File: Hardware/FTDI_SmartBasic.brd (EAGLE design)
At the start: 35.6 x 20.3 mm, 27 parts, among them U1 FT232RLSSOP, U2 MIC5219 3.3V, U3 TS3USB221A

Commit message: Ready for release.
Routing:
- net !OE: track 14.0 -> 16.4 mm
- net N$17: track 16.9 -> 15.9 mm
- net N$16: track 19.7 -> 18.9 mm
- net GND: vias 10 -> 9
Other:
- board text added: "HOST/!USB"
- board text removed: "AUX/!USB"
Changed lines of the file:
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@@
 <grid distance="0.05" unitdist="inch" unit="inch" style="lines" multiple="1" display="yes" altdistance="0.005" altunitdist="inch" altunit="inch"/>
 <layers>
-<layer number="1" name="Top" color="4" fill="1" visible="yes" active="yes"/>
+<layer number="1" name="Top" color="4" fill="1" visible="no" active="yes"/>
 <layer number="2" name="Route2" color="1" fill="3" visible="no" active="yes"/>
 <layer number="15" name="Route15" color="4" fill="6" visible="no" active="yes"/>
@@
 <layer number="19" name="Unrouted" color="6" fill="1" visible="yes" active="yes"/>
 <layer number="20" name="Dimension" color="15" fill="1" visible="yes" active="yes"/>
-<layer number="21" name="tPlace" color="16" fill="1" visible="yes" active="yes"/>
+<layer number="21" name="tPlace" color="16" fill="1" visible="no" active="yes"/>
 <layer number="22" name="bPlace" color="14" fill="1" visible="yes" active="yes"/>
-<layer number="23" name="tOrigins" color="15" fill="1" visible="yes" active="yes"/>
+<layer number="23" name="tOrigins" color="15" fill="1" visible="no" active="yes"/>
 <layer number="24" name="bOrigins" color="15" fill="1" visible="yes" active="yes"/>
 <layer number="25" name="tNames" color="7" fill="1" visible="no" active="yes"/>
@@
 <layer number="43" name="vRestrict" color="2" fill="10" visible="no" active="yes"/>
 <layer number="44" name="Drills" color="7" fill="1" visible="no" active="yes"/>
-<layer number="45" name="Holes" color="7" fill="1" visible="yes" active="yes"/>
+<layer number="45" name="Holes" color="7" fill="1" visible="no" active="yes"/>
 <layer number="46" name="Milling" color="3" fill="1" visible="no" active="yes"/>
-<layer number="51" name="tDocu" color="6" fill="1" visible="yes" active="yes"/>
+<layer number="51" name="tDocu" color="6" fill="1" visible="no" active="yes"/>
 <layer number="52" name="bDocu" color="7" fill="1" visible="no" active="yes"/>
 <layer number="3" name="Route3" color="4" fill="3" visible="no" active="no"/>
@@
 <text x="26.797" y="11.938" size="0.8636" layer="21" font="vector" ratio="15" align="bottom-center">TX</text>
 <text x="24.765" y="11.938" size="0.8636" layer="21" font="vector" ratio="15" align="bottom-center">RX</text>
-<text x="27.94" y="6.35" size="1.016" layer="21" font="vector" ratio="15" rot="R180" align="bottom-center">AUX/!USB</text>
+<text x="27.94" y="6.35" size="1.016" layer="21" font="vector" ratio="15" rot="R180" align="bottom-center">HOST/!USB</text>
 <text x="27.94" y="3.048" size="0.8636" layer="21" font="vector" ratio="15" align="bottom-center">SEL</text>
 <text x="30.48" y="3.048" size="0.8636" layer="21" font="vector" ratio="15" align="bottom-center">!OE</text>
@@
 <via x="17.526" y="15.367" extent="1-16" drill="0.508"/>
 <via x="5.842" y="16.256" extent="1-16" drill="0.508"/>
-<via x="15.621" y="17.907" extent="1-16" drill="0.508"/>
+<via x="15.24" y="17.78" extent="1-16" drill="0.508"/>
 <via x="15.494" y="8.001" extent="1-16" drill="0.508"/>
 <contactref element="R3" pad="1"/>
 <contactref element="R5" pad="1"/>
 <contactref element="C6" pad="2"/>
-<via x="26.543" y="5.969" extent="1-16" drill="0.508"/>
 <via x="28.067" y="10.033" extent="1-16" drill="0.508"/>
 </signal>
@@
 <contactref element="R1" pad="2"/>
 <contactref element="R2" pad="2"/>
-<wire x1="13.97" y1="16.93" x2="18.415" y2="17.018" width="0.254" layer="1"/>
-<wire x1="18.415" y1="17.018" x2="18.962" y2="17.565" width="0.254" layer="1"/>
+<wire x1="18.327" y1="16.93" x2="18.962" y2="17.565" width="0.254" layer="1"/>
 <wire x1="18.962" y1="17.565" x2="20.232" y2="17.565" width="0.254" layer="1"/>
 <wire x1="20.232" y1="17.565" x2="20.828" y2="16.764" width="0.254" layer="1"/>
@@
 <wire x1="25.058" y1="10.287" x2="25.058" y2="9.564" width="0.254" layer="1"/>
 <wire x1="25.058" y1="9.564" x2="25.019" y2="9.525" width="0.254" layer="1"/>
+<wire x1="13.97" y1="16.93" x2="18.327" y2="16.93" width="0.254" layer="1"/>
 </signal>
 <signal name="N$5">
@@
 <wire x1="28.436" y1="8.624" x2="28.956" y2="9.144" width="0.254" layer="1"/>
 <via x="28.956" y="9.144" extent="1-16" drill="0.508"/>
-<wire x1="27.94" y1="6.35" x2="28.321" y2="6.731" width="0.254" layer="16"/>
+<wire x1="27.94" y1="6.223" x2="28.321" y2="6.731" width="0.254" layer="16"/>
 <wire x1="28.321" y1="6.731" x2="28.956" y2="6.731" width="0.254" layer="16"/>
 <wire x1="28.956" y1="6.731" x2="28.956" y2="9.144" width="0.254" layer="16"/>
@@
 <contactref element="D4" pad="A"/>
 <wire x1="28.956" y1="9.144" x2="28.956" y2="11.215" width="0.254" layer="1"/>
-<wire x1="27.94" y1="6.35" x2="27.94" y2="5.969" width="0.254" layer="16"/>
-<via x="27.94" y="5.969" extent="1-16" drill="0.508"/>
-<wire x1="27.94" y1="5.969" x2="27.94" y2="4.572" width="0.254" layer="1"/>
+<via x="27.94" y="6.223" extent="1-16" drill="0.381"/>
 <wire x1="27.94" y1="4.572" x2="27.94" y2="1.27" width="0.254" layer="1"/>
 <wire x1="28.817" y1="4.699" x2="28.067" y2="4.699" width="0.254" layer="1"/>
 <wire x1="28.067" y1="4.699" x2="27.94" y2="4.572" width="0.2032" layer="1"/>
+<wire x1="27.94" y1="6.223" x2="27.94" y2="4.826" width="0.254" layer="1"/>
+<wire x1="27.94" y1="4.826" x2="28.067" y2="4.699" width="0.254" layer="1"/>
 </signal>
 <signal name="!OE">
@@
 <contactref element="JP2" pad="1"/>
 <via x="30.353" y="9.652" extent="1-16" drill="0.508"/>
-<wire x1="26.635" y1="7.124" x2="29.198" y2="7.124" width="0.254" layer="1"/>
-<wire x1="29.198" y1="7.124" x2="29.972" y2="6.35" width="0.254" layer="1"/>
-<wire x1="29.972" y1="6.35" x2="30.48" y2="5.842" width="0.254" layer="1"/>
-<wire x1="30.48" y1="1.27" x2="30.48" y2="5.842" width="0.254" layer="1"/>
+<wire x1="26.635" y1="7.124" x2="28.702" y2="7.124" width="0.254" layer="1"/>
+<wire x1="28.702" y1="7.124" x2="29.198" y2="7.124" width="0.254" layer="1"/>
+<wire x1="30.48" y1="1.27" x2="30.48" y2="4.699" width="0.254" layer="1"/>
 <wire x1="30.353" y1="9.652" x2="30.353" y2="11.215" width="0.254" layer="1"/>
-<wire x1="30.353" y1="9.652" x2="30.353" y2="6.731" width="0.2032" layer="16"/>
-<wire x1="30.353" y1="6.731" x2="29.972" y2="6.35" width="0.2032" layer="16"/>
-<via x="29.972" y="6.35" extent="1-16" drill="0.508"/>
+<wire x1="30.353" y1="9.652" x2="30.353" y2="5.842" width="0.2032" layer="16"/>
+<via x="30.48" y="4.699" extent="1-16" drill="0.508"/>
+<wire x1="30.48" y1="6.477" x2="29.845" y2="7.112" width="0.254" layer="1"/>
+<wire x1="29.845" y1="7.112" x2="28.714" y2="7.112" width="0.254" layer="1"/>
+<wire x1="28.714" y1="7.112" x2="28.702" y2="7.124" width="0.254" layer="1"/>
+<wire x1="30.353" y1="5.842" x2="30.48" y2="5.715" width="0.2032" layer="16"/>
+<wire x1="30.48" y1="5.715" x2="30.48" y2="4.699" width="0.2032" layer="16"/>
+<wire x1="30.48" y1="6.477" x2="30.48" y2="4.699" width="0.254" layer="1"/>
 </signal>
 <signal name="N$13">
@@
 <wire x1="25.435" y1="7.624" x2="24.388" y2="7.624" width="0.254" layer="1"/>
 <wire x1="24.388" y1="7.624" x2="24.003" y2="7.239" width="0.254" layer="1"/>
-<wire x1="24.003" y1="7.239" x2="24.003" y2="4.191" width="0.254" layer="1"/>
-<wire x1="24.003" y1="4.191" x2="23.622" y2="3.81" width="0.254" layer="1"/>
-<wire x1="23.622" y1="3.81" x2="12.7" y2="3.81" width="0.254" layer="1"/>
+<wire x1="24.003" y1="7.239" x2="24.003" y2="5.461" width="0.254" layer="1"/>
+<wire x1="24.003" y1="5.461" x2="23.622" y2="5.08" width="0.254" layer="1"/>
+<wire x1="23.622" y1="5.08" x2="23.241" y2="5.08" width="0.254" layer="1"/>
+<wire x1="23.241" y1="5.08" x2="21.971" y2="3.81" width="0.254" layer="1"/>
+<wire x1="21.971" y1="3.81" x2="12.7" y2="3.81" width="0.254" layer="1"/>
 <wire x1="12.7" y1="3.81" x2="10.16" y2="1.27" width="0.254" layer="1"/>
 </signal>
@@
 <wire x1="25.435" y1="7.124" x2="25.158" y2="7.124" width="0.254" layer="1"/>
 <wire x1="25.158" y1="7.124" x2="24.638" y2="6.604" width="0.254" layer="1"/>
-<wire x1="24.638" y1="6.604" x2="24.638" y2="3.683" width="0.254" layer="1"/>
-<wire x1="24.638" y1="3.683" x2="23.876" y2="2.921" width="0.254" layer="1"/>
-<wire x1="23.876" y1="2.921" x2="14.351" y2="2.921" width="0.254" layer="1"/>
+<wire x1="24.638" y1="6.604" x2="24.638" y2="5.334" width="0.254" layer="1"/>
+<wire x1="24.638" y1="5.334" x2="23.749" y2="4.445" width="0.254" layer="1"/>
+<wire x1="23.749" y1="4.445" x2="23.495" y2="4.445" width="0.254" layer="1"/>
+<wire x1="23.495" y1="4.445" x2="21.971" y2="2.921" width="0.254" layer="1"/>
+<wire x1="21.971" y1="2.921" x2="14.351" y2="2.921" width="0.254" layer="1"/>
 <wire x1="14.351" y1="2.921" x2="12.7" y2="1.27" width="0.254" layer="1"/>
 </signal>
@@
 <wire x1="21.082" y1="15.621" x2="21.082" y2="16.002" width="0.254" layer="16"/>
 <wire x1="21.082" y1="16.002" x2="21.59" y2="16.51" width="0.254" layer="16"/>
-<wire x1="21.59" y1="16.51" x2="29.591" y2="16.51" width="0.254" layer="16"/>
-<wire x1="29.591" y1="16.51" x2="30.226" y2="17.145" width="0.254" layer="16"/>
-<via x="30.226" y="17.145" extent="1-16" drill="0.508"/>
-<wire x1="30.226" y1="17.145" x2="31.115" y2="17.145" width="0.254" layer="1"/>
+<wire x1="21.59" y1="16.51" x2="28.575" y2="16.51" width="0.254" layer="16"/>
+<wire x1="28.575" y1="16.51" x2="29.21" y2="17.145" width="0.254" layer="16"/>
+<via x="29.21" y="17.145" extent="1-16" drill="0.508"/>
+<wire x1="29.21" y1="17.145" x2="31.115" y2="17.145" width="0.254" layer="1"/>
 <wire x1="31.115" y1="17.145" x2="31.75" y2="16.51" width="0.254" layer="1"/>
 <wire x1="31.75" y1="16.51" x2="34.29" y2="16.51" width="0.254" layer="1"/>

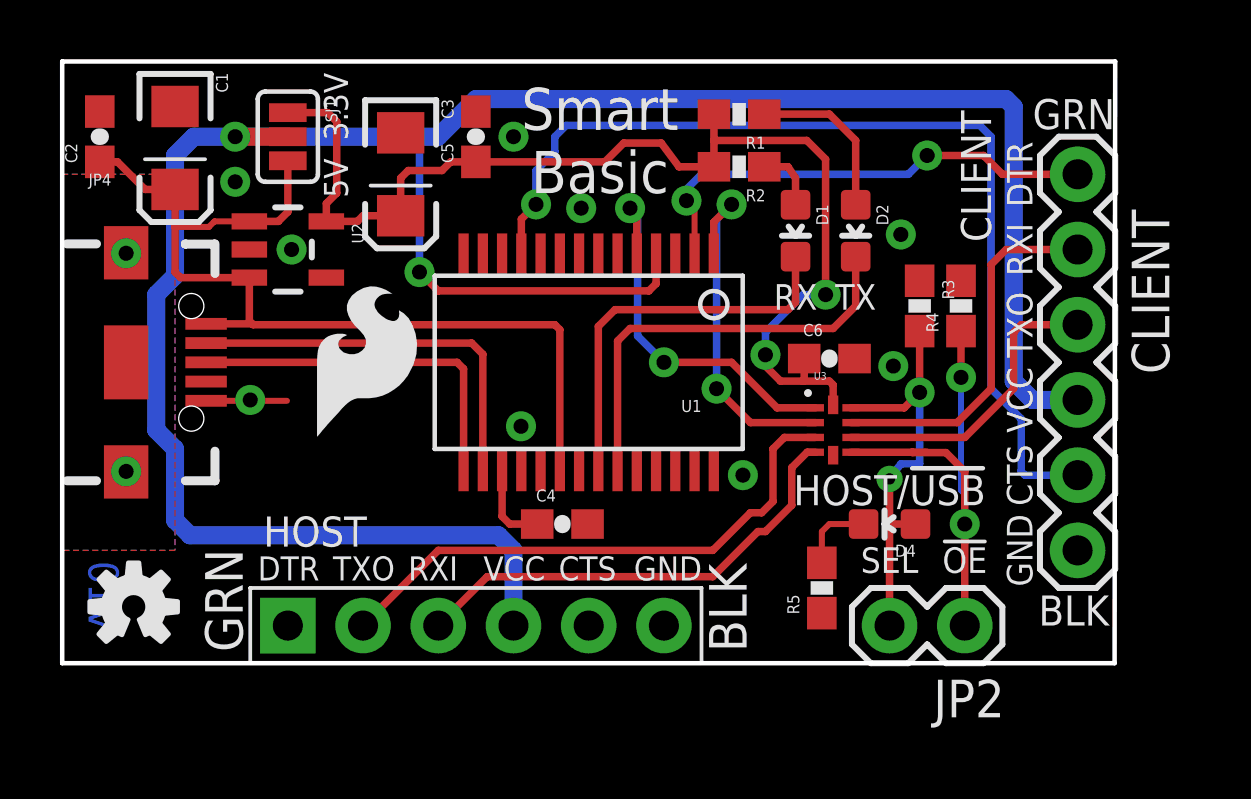
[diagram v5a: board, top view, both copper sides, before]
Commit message: added local fiducials
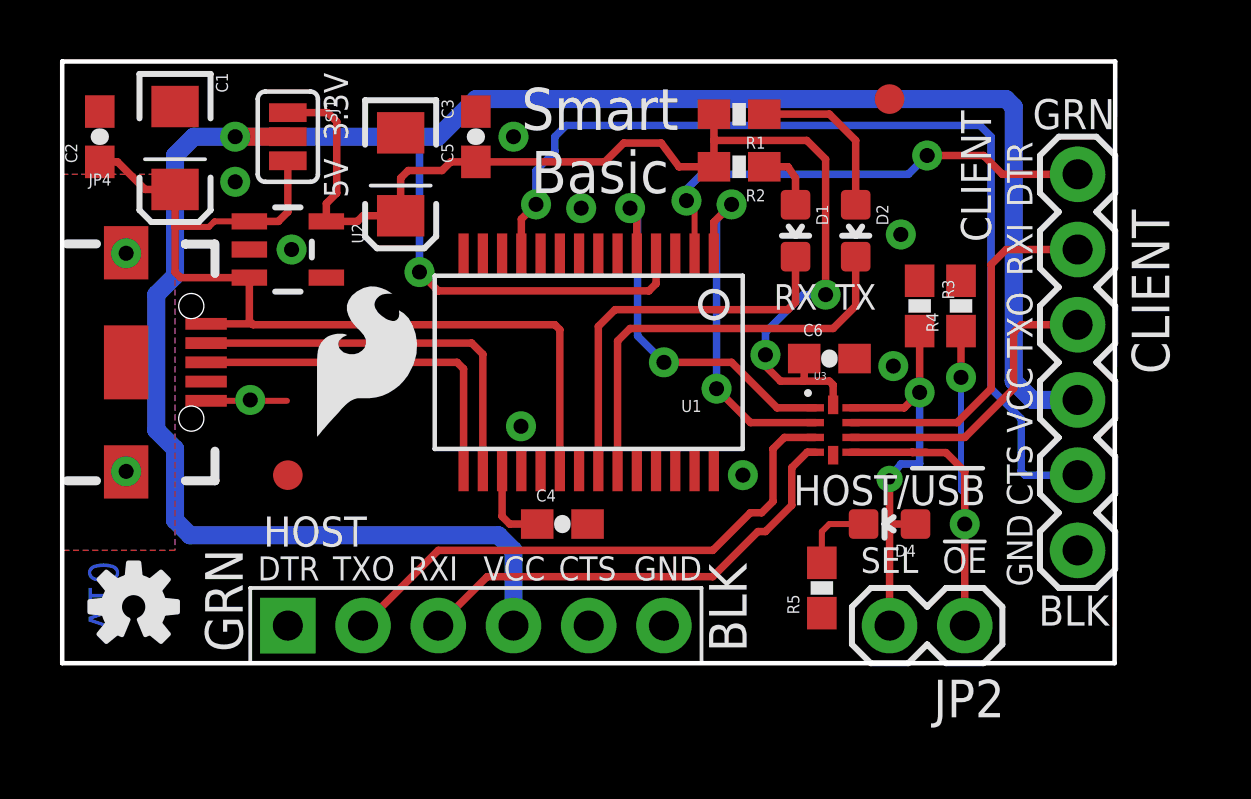
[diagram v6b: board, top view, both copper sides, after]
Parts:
- added FID1, FID2: FIDUCIAL1X2, SparkFun-Aesthetics:FIDUCIAL-1X2
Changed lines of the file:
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@@
 <?xml version="1.0" encoding="utf-8"?>
 <!DOCTYPE eagle SYSTEM "eagle.dtd">
-<eagle version="6.5.0">
+<eagle version="6.6.0">
 <drawing>
 <settings>
@@
 <setting verticaltext="up"/>
 </settings>
-<grid distance="0.05" unitdist="inch" unit="inch" style="lines" multiple="1" display="yes" altdistance="0.005" altunitdist="inch" altunit="inch"/>
+<grid distance="0.05" unitdist="inch" unit="inch" style="lines" multiple="1" display="yes" altdistance="0.01" altunitdist="inch" altunit="inch"/>
 <layers>
-<layer number="1" name="Top" color="4" fill="1" visible="no" active="yes"/>
-<layer number="2" name="Route2" color="1" fill="3" visible="no" active="yes"/>
-<layer number="15" name="Route15" color="4" fill="6" visible="no" active="yes"/>
+<layer number="1" name="Top" color="4" fill="1" visible="yes" active="yes"/>
+<layer number="2" name="Route2" color="1" fill="3" visible="yes" active="yes"/>
+<layer number="15" name="Route15" color="4" fill="6" visible="yes" active="yes"/>
 <layer number="16" name="Bottom" color="1" fill="1" visible="yes" active="yes"/>
 <layer number="17" name="Pads" color="2" fill="1" visible="yes" active="yes"/>
 <layer number="18" name="Vias" color="2" fill="1" visible="yes" active="yes"/>
 <layer number="19" name="Unrouted" color="6" fill="1" visible="yes" active="yes"/>
-<layer number="20" name="Dimension" color="15" fill="1" visible="yes" active="yes"/>
-<layer number="21" name="tPlace" color="16" fill="1" visible="no" active="yes"/>
-<layer number="22" name="bPlace" color="14" fill="1" visible="yes" active="yes"/>
-<layer number="23" name="tOrigins" color="15" fill="1" visible="no" active="yes"/>
+<layer number="20" name="Dimension" color="6" fill="1" visible="yes" active="yes"/>
+<layer number="21" name="tPlace" color="6" fill="1" visible="yes" active="yes"/>
+<layer number="22" name="bPlace" color="6" fill="1" visible="yes" active="yes"/>
+<layer number="23" name="tOrigins" color="15" fill="1" visible="yes" active="yes"/>
 <layer number="24" name="bOrigins" color="15" fill="1" visible="yes" active="yes"/>
-<layer number="25" name="tNames" color="7" fill="1" visible="no" active="yes"/>
-<layer number="26" name="bNames" color="7" fill="1" visible="no" active="yes"/>
-<layer number="27" name="tValues" color="7" fill="1" visible="no" active="yes"/>
-<layer number="28" name="bValues" color="7" fill="1" visible="no" active="yes"/>
-<layer number="29" name="tStop" color="7" fill="3" visible="no" active="yes"/>
-<layer number="30" name="bStop" color="7" fill="6" visible="no" active="yes"/>
-<layer number="31" name="tCream" color="7" fill="4" visible="no" active="yes"/>
-<layer number="32" name="bCream" color="7" fill="5" visible="no" active="yes"/>
-<layer number="39" name="tKeepout" color="4" fill="11" visible="no" active="yes"/>
-<layer number="40" name="bKeepout" color="1" fill="11" visible="no" active="yes"/>
-<layer number="41" name="tRestrict" color="4" fill="10" visible="no" active="yes"/>
-<layer number="42" name="bRestrict" color="1" fill="10" visible="no" active="yes"/>
-<layer number="43" name="vRestrict" color="2" fill="10" visible="no" active="yes"/>
-<layer number="44" name="Drills" color="7" fill="1" visible="no" active="yes"/>
-<layer number="45" name="Holes" color="7" fill="1" visible="no" active="yes"/>
-<layer number="46" name="Milling" color="3" fill="1" visible="no" active="yes"/>
-<layer number="51" name="tDocu" color="6" fill="1" visible="no" active="yes"/>
-<layer number="52" name="bDocu" color="7" fill="1" visible="no" active="yes"/>
+<layer number="25" name="tNames" color="7" fill="1" visible="yes" active="yes"/>
+<layer number="26" name="bNames" color="7" fill="1" visible="yes" active="yes"/>
+<layer number="27" name="tValues" color="7" fill="1" visible="yes" active="yes"/>
+<layer number="28" name="bValues" color="7" fill="1" visible="yes" active="yes"/>
+<layer number="29" name="tStop" color="7" fill="3" visible="yes" active="yes"/>
+<layer number="30" name="bStop" color="7" fill="6" visible="yes" active="yes"/>
+<layer number="31" name="tCream" color="7" fill="4" visible="yes" active="yes"/>
+<layer number="32" name="bCream" color="7" fill="5" visible="yes" active="yes"/>
+<layer number="39" name="tKeepout" color="4" fill="11" visible="yes" active="yes"/>
+<layer number="40" name="bKeepout" color="1" fill="11" visible="yes" active="yes"/>
+<layer number="41" name="tRestrict" color="4" fill="10" visible="yes" active="yes"/>
+<layer number="42" name="bRestrict" color="1" fill="10" visible="yes" active="yes"/>
+<layer number="43" name="vRestrict" color="2" fill="10" visible="yes" active="yes"/>
+<layer number="44" name="Drills" color="7" fill="1" visible="yes" active="yes"/>
+<layer number="45" name="Holes" color="7" fill="1" visible="yes" active="yes"/>
+<layer number="46" name="Milling" color="3" fill="1" visible="yes" active="yes"/>
+<layer number="51" name="tDocu" color="6" fill="1" visible="yes" active="yes"/>
+<layer number="52" name="bDocu" color="7" fill="1" visible="yes" active="yes"/>
 <layer number="3" name="Route3" color="4" fill="3" visible="no" active="no"/>
 <layer number="4" name="Route4" color="1" fill="4" visible="no" active="no"/>
@@
 <element name="LOGO3" library="SparkFun-Aesthetics" package="OSHW-LOGO-S" value="OSHW-LOGOS" x="2.413" y="1.905"/>
 <element name="LOGO2" library="SparkFun-Aesthetics" package="SFE_LOGO_FLAME_.2" value="SFE_LOGO_FLAME.2_INCH" x="8.255" y="7.366"/>
+<element name="FID1" library="SparkFun-Aesthetics" package="FIDUCIAL-1X2" value="FIDUCIAL1X2" x="7.62" y="6.35"/>
+<element name="FID2" library="SparkFun-Aesthetics" package="FIDUCIAL-1X2" value="FIDUCIAL1X2" x="27.94" y="19.05"/>
 </elements>
 <signals>
